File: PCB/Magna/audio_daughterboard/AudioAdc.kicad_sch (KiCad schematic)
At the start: 23 parts, among them J201 PSG01550, U201 WM8782SEDS

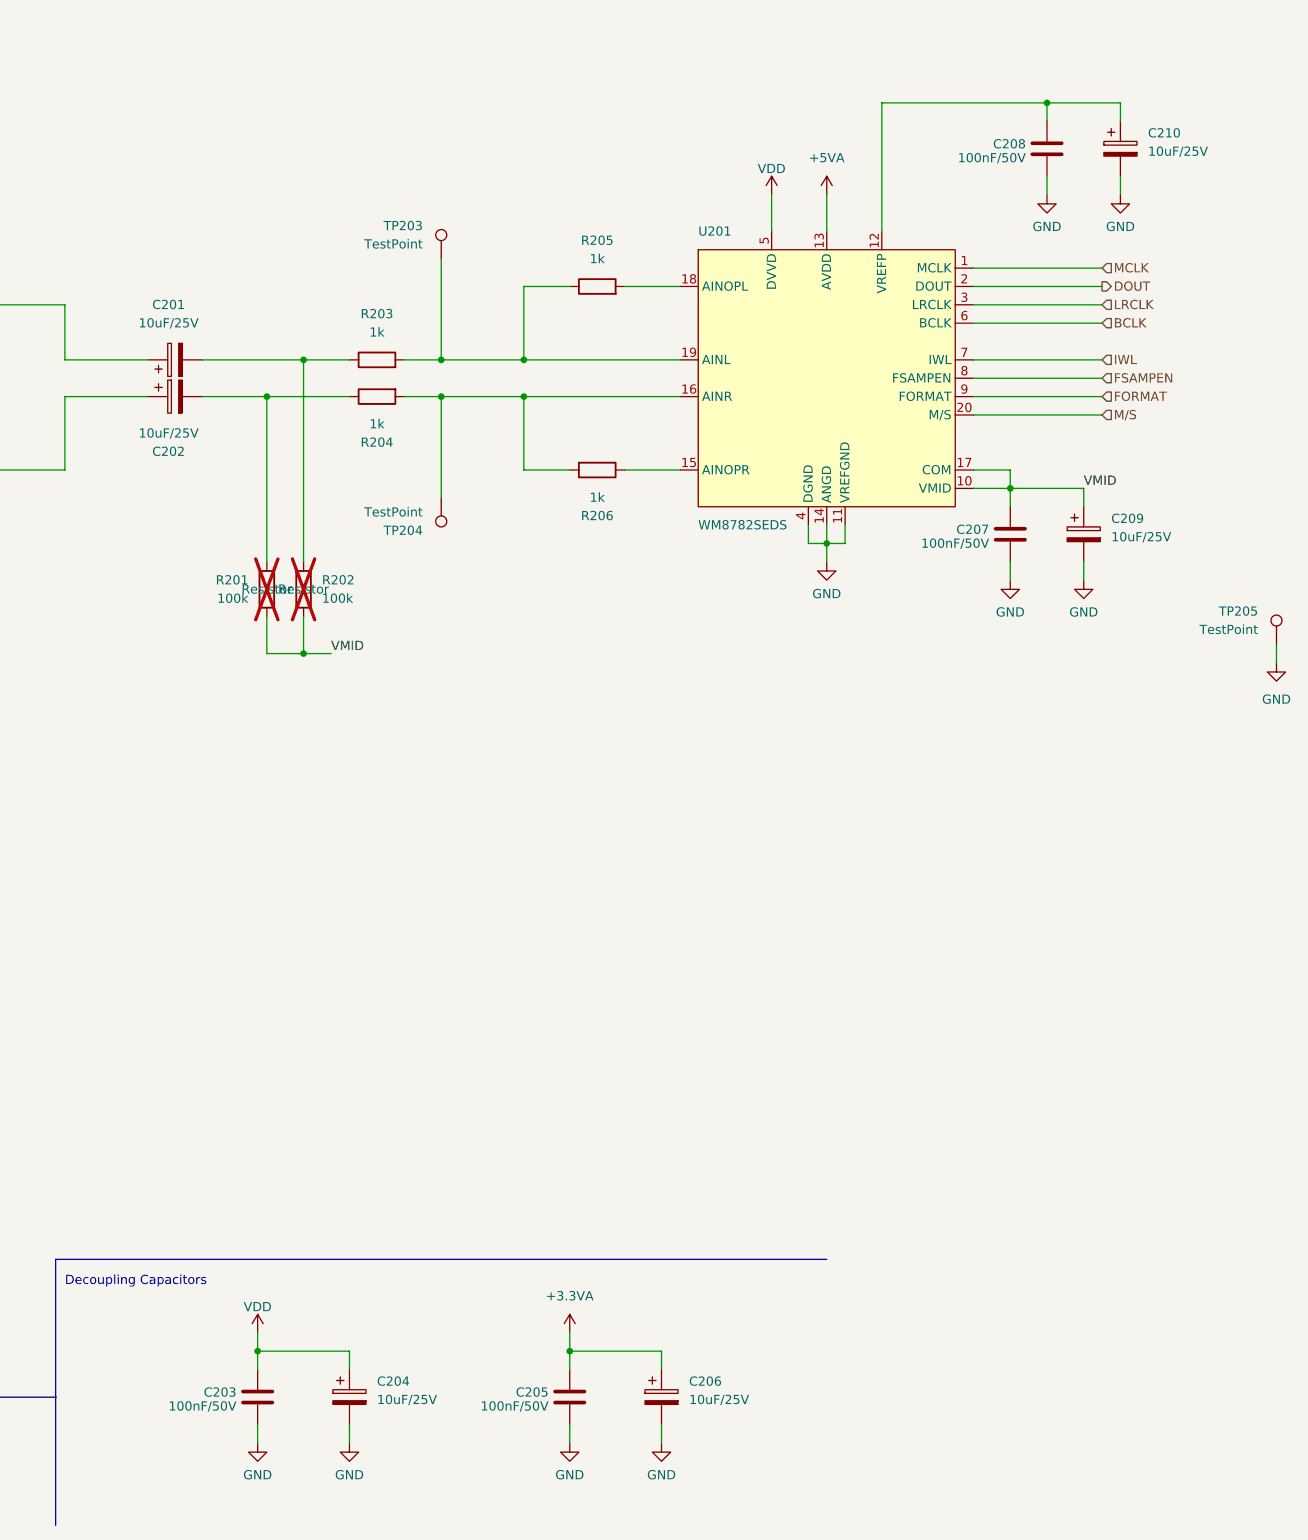
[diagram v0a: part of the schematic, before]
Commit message: Update audio PCB
Mainly added simulations to Linedriver and DAC.

Also fixed some small issues that was found when simulating
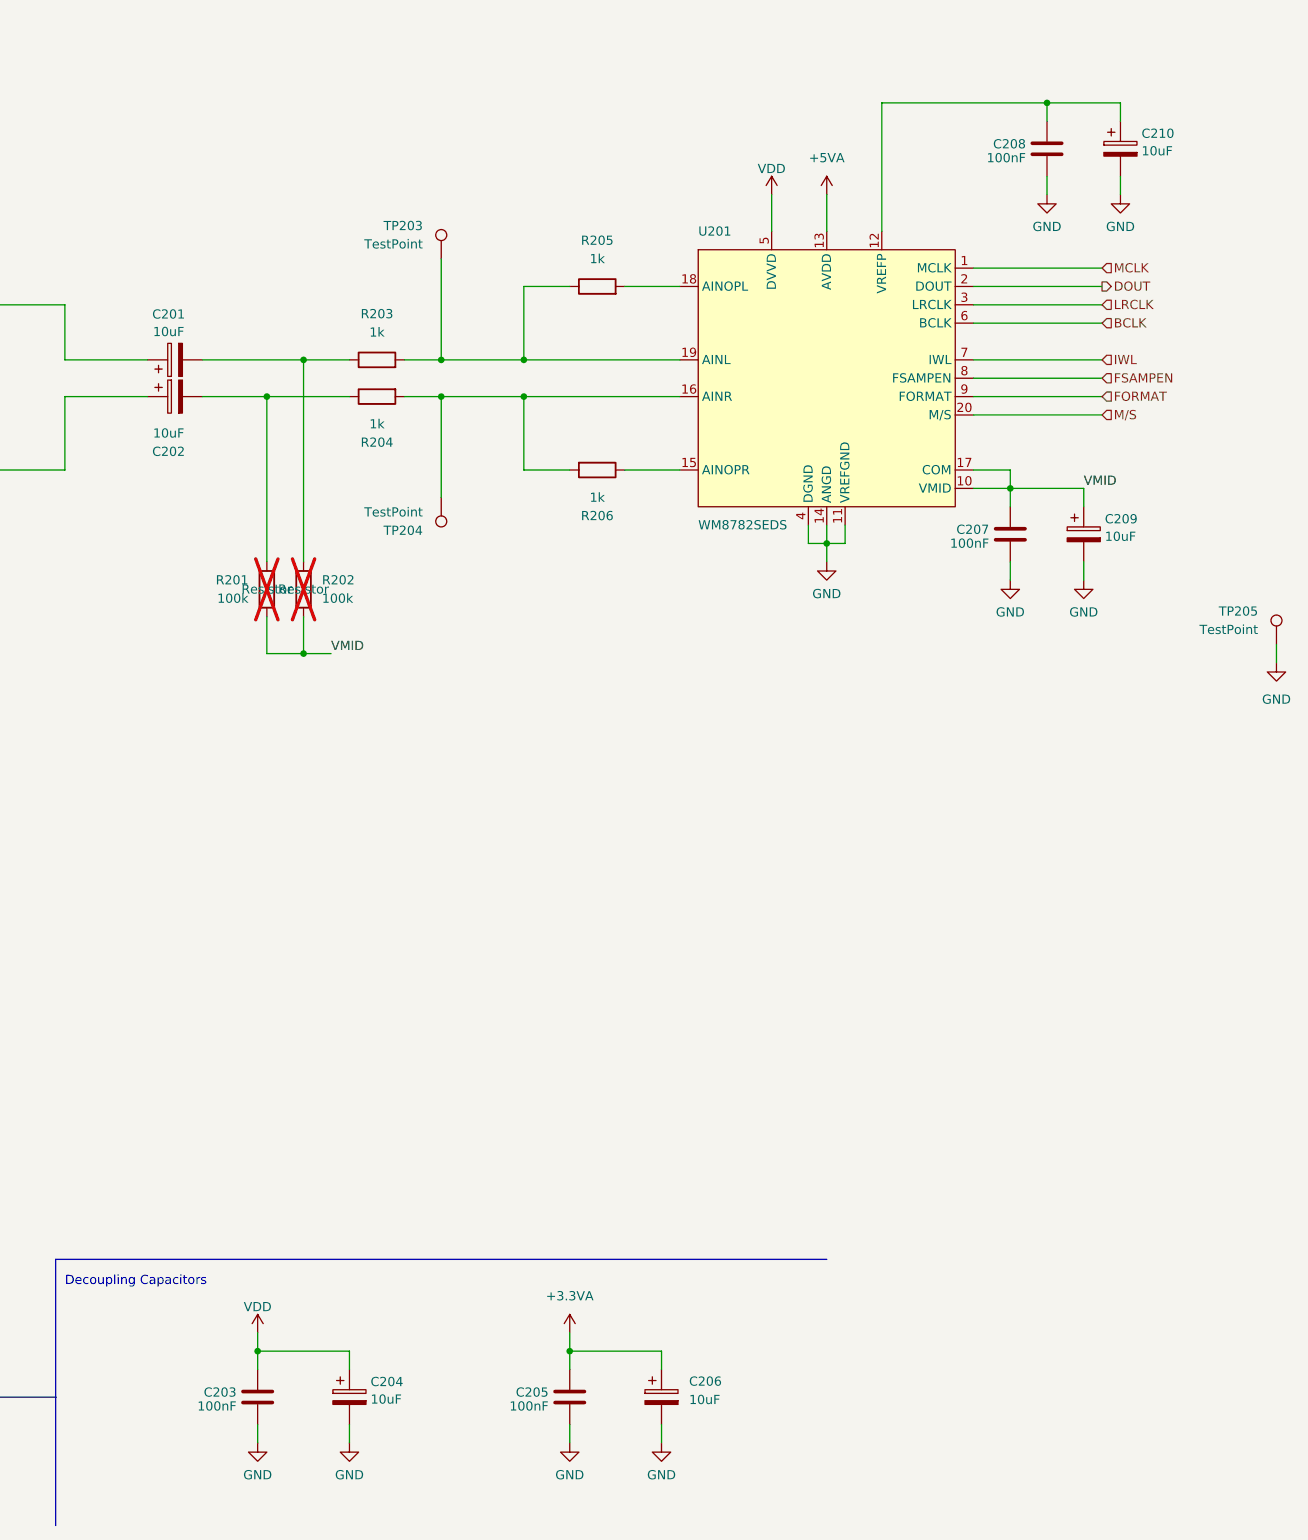
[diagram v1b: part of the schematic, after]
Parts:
- C201, C202, C204, C206, C209, C210: value 10uF/25V -> 10uF
- C203, C205, C207, C208: value 100nF/50V -> 100nF
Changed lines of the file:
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@@
 		(fields_autoplaced yes)
 		(property "Reference" "C210"
-			(at 359.41 66.421 0)
-			(effects
-				(font
-					(size 1.27 1.27)
-				)
-				(justify left)
-			)
-		)
-		(property "Value" "10uF/25V"
-			(at 359.41 68.961 0)
+			(at 358.521 66.4788 0)
+			(effects
+				(font
+					(size 1.27 1.27)
+				)
+				(justify left)
+			)
+		)
+		(property "Value" "10uF"
+			(at 358.521 68.9031 0)
 			(effects
 				(font
@@
 			)
 		)
-		(property "Value" "100nF/50V"
+		(property "Value" "100nF"
 			(at 342.519 69.8573 0)
 			(effects
@@
 			)
 		)
-		(property "Value" "100nF/50V"
+		(property "Value" "100nF"
 			(at 276.479 242.5773 0)
 			(effects
@@
 			)
 		)
-		(property "Value" "10uF/25V"
+		(property "Value" "10uF"
 			(at 295.91 241.681 0)
 			(effects
@@
 		(fields_autoplaced yes)
 		(property "Reference" "C201"
-			(at 223.901 90.17 90)
-			(effects
-				(font
-					(size 1.27 1.27)
-				)
-			)
-		)
-		(property "Value" "10uF/25V"
-			(at 223.901 92.71 90)
+			(at 223.901 91.4865 90)
+			(effects
+				(font
+					(size 1.27 1.27)
+				)
+			)
+		)
+		(property "Value" "10uF"
+			(at 223.901 93.9108 90)
 			(effects
 				(font
@@
 			)
 		)
-		(property "Value" "100nF/50V"
+		(property "Value" "100nF"
 			(at 337.439 123.1973 0)
 			(effects
@@
 			)
 		)
-		(property "Value" "10uF/25V"
+		(property "Value" "10uF"
 			(at 223.901 107.95 90)
 			(effects
@@
 		(fields_autoplaced yes)
 		(property "Reference" "C204"
-			(at 252.73 239.141 0)
-			(effects
-				(font
-					(size 1.27 1.27)
-				)
-				(justify left)
-			)
-		)
-		(property "Value" "10uF/25V"
-			(at 252.73 241.681 0)
+			(at 251.841 239.1988 0)
+			(effects
+				(font
+					(size 1.27 1.27)
+				)
+				(justify left)
+			)
+		)
+		(property "Value" "10uF"
+			(at 251.841 241.6231 0)
 			(effects
 				(font
@@
 			)
 		)
-		(property "Value" "100nF/50V"
+		(property "Value" "100nF"
 			(at 233.299 242.5773 0)
 			(effects
@@
 		(fields_autoplaced yes)
 		(property "Reference" "C209"
-			(at 354.33 119.761 0)
-			(effects
-				(font
-					(size 1.27 1.27)
-				)
-				(justify left)
-			)
-		)
-		(property "Value" "10uF/25V"
-			(at 354.33 122.301 0)
-			(effects
-				(font
+			(at 353.441 119.8188 0)
+			(effects
+				(font
+					(size 1.27 1.27)
+				)
+				(justify left)
+			)
+		)
+		(property "Value" "10uF"
+			(at 353.441 122.2431 0)
+			(effects
+				(font

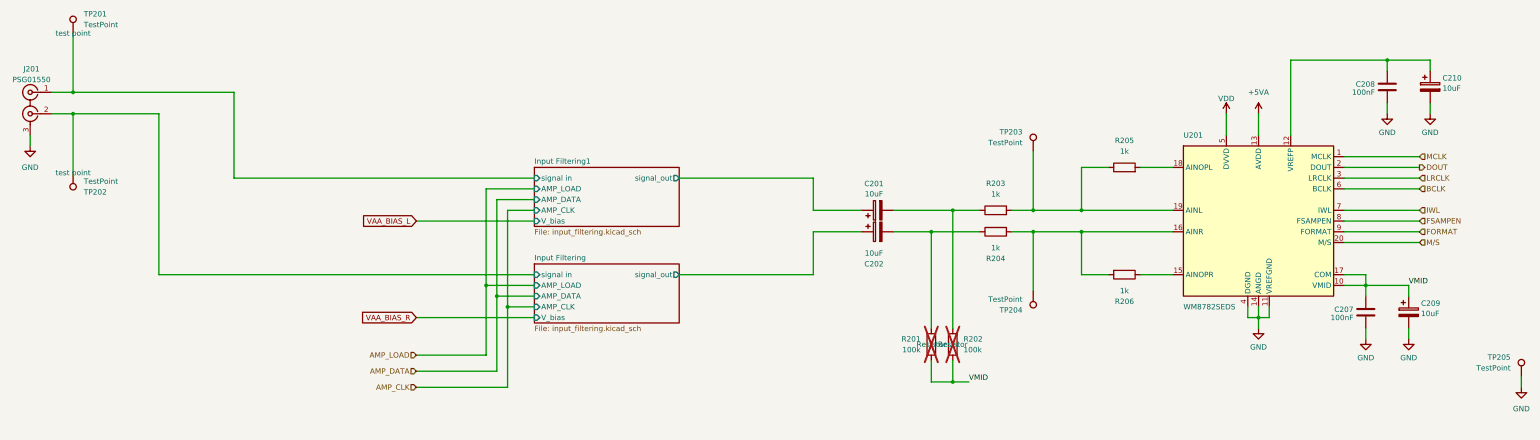
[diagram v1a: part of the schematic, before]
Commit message: "Finalize" Audio daugherboard
Finished DAC output filter
Fixed the whole damn MCU subschematic
Fixed Linedriver schematic
Added component footprints and LCSC numbers
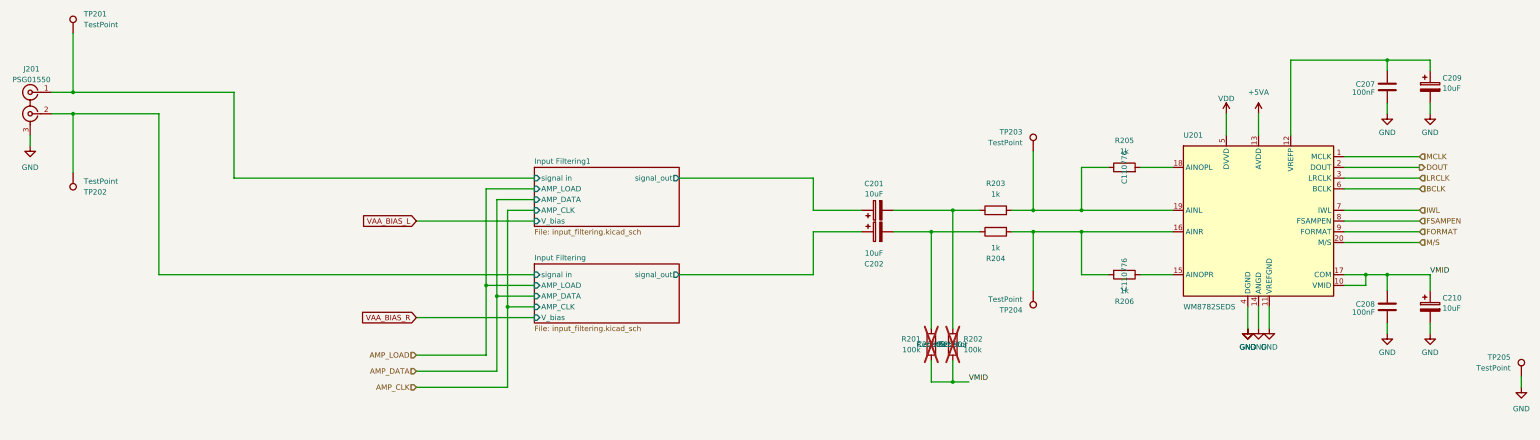
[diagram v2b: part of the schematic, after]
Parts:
- C201, C202, C203, C204, C205, C206, J201, TP201, TP202, TP203, TP204, TP205, U201: now left out of the parts list
- C207: renamed from C208; now left out of the parts list
- C208: renamed from C207; now left out of the parts list
- C209: renamed from C210; now left out of the parts list
- C210: renamed from C209; now left out of the parts list
- R201, R202: footprint (none) -> Resistor_SMD:R_0603_1608Metric; LCSC (none) -> C25803
- R203, R204, R205, R206: footprint (none) -> Resistor_SMD:R_0603_1608Metric; LCSC (none) -> C110776; now left out of the parts list
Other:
- moved on the sheet: C208, C210

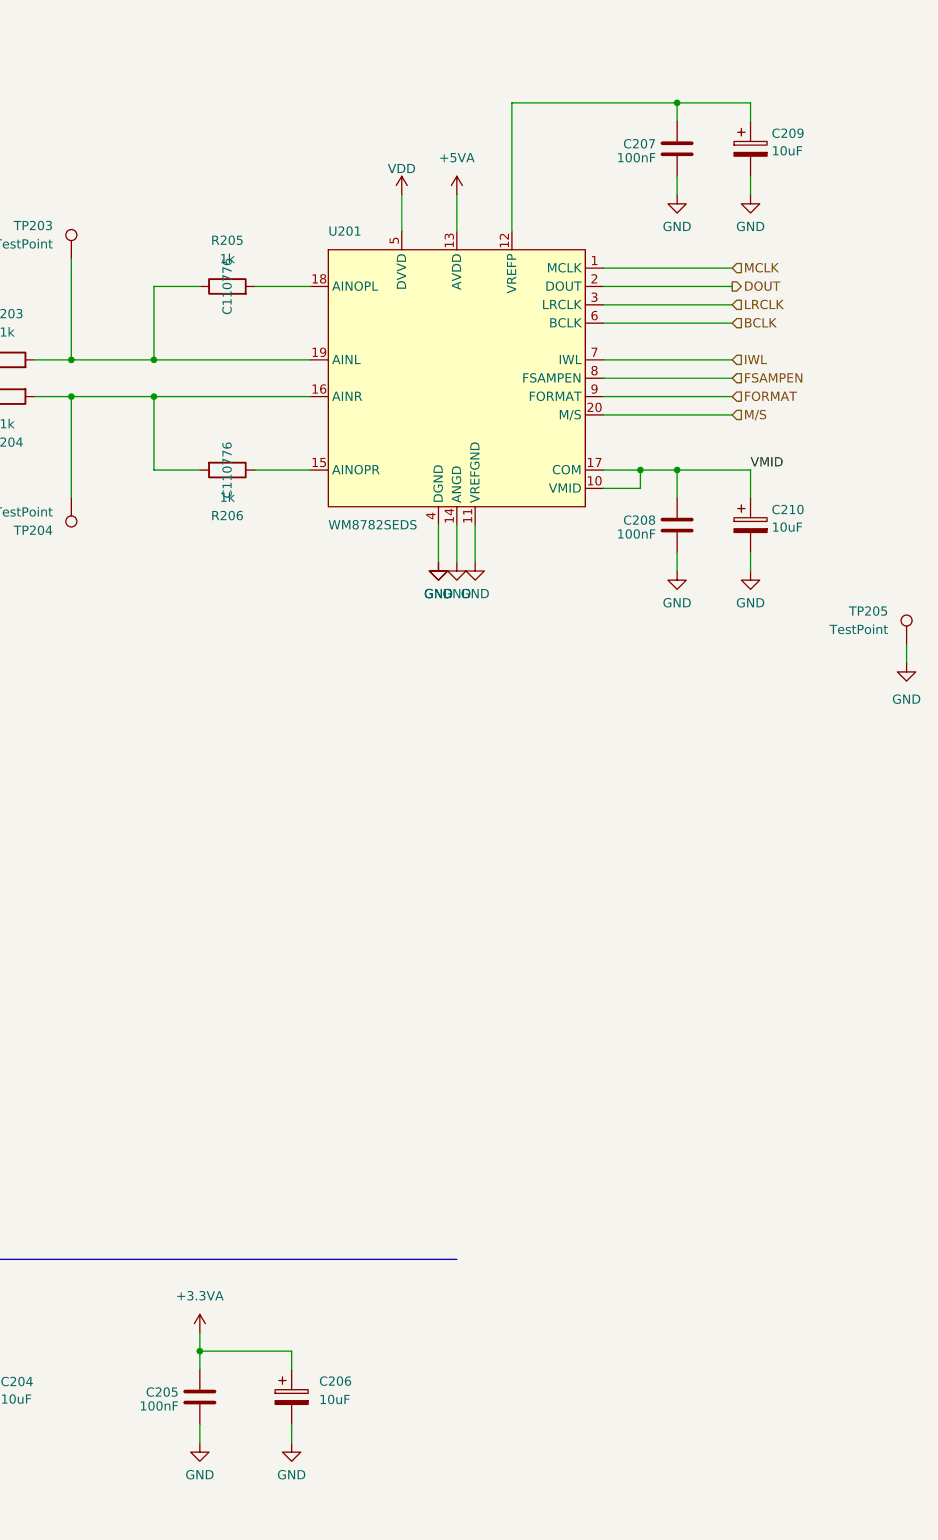
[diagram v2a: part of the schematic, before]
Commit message: Do most of the component placement for audio board
Just a general layout, things will probably change
as the routing begins.
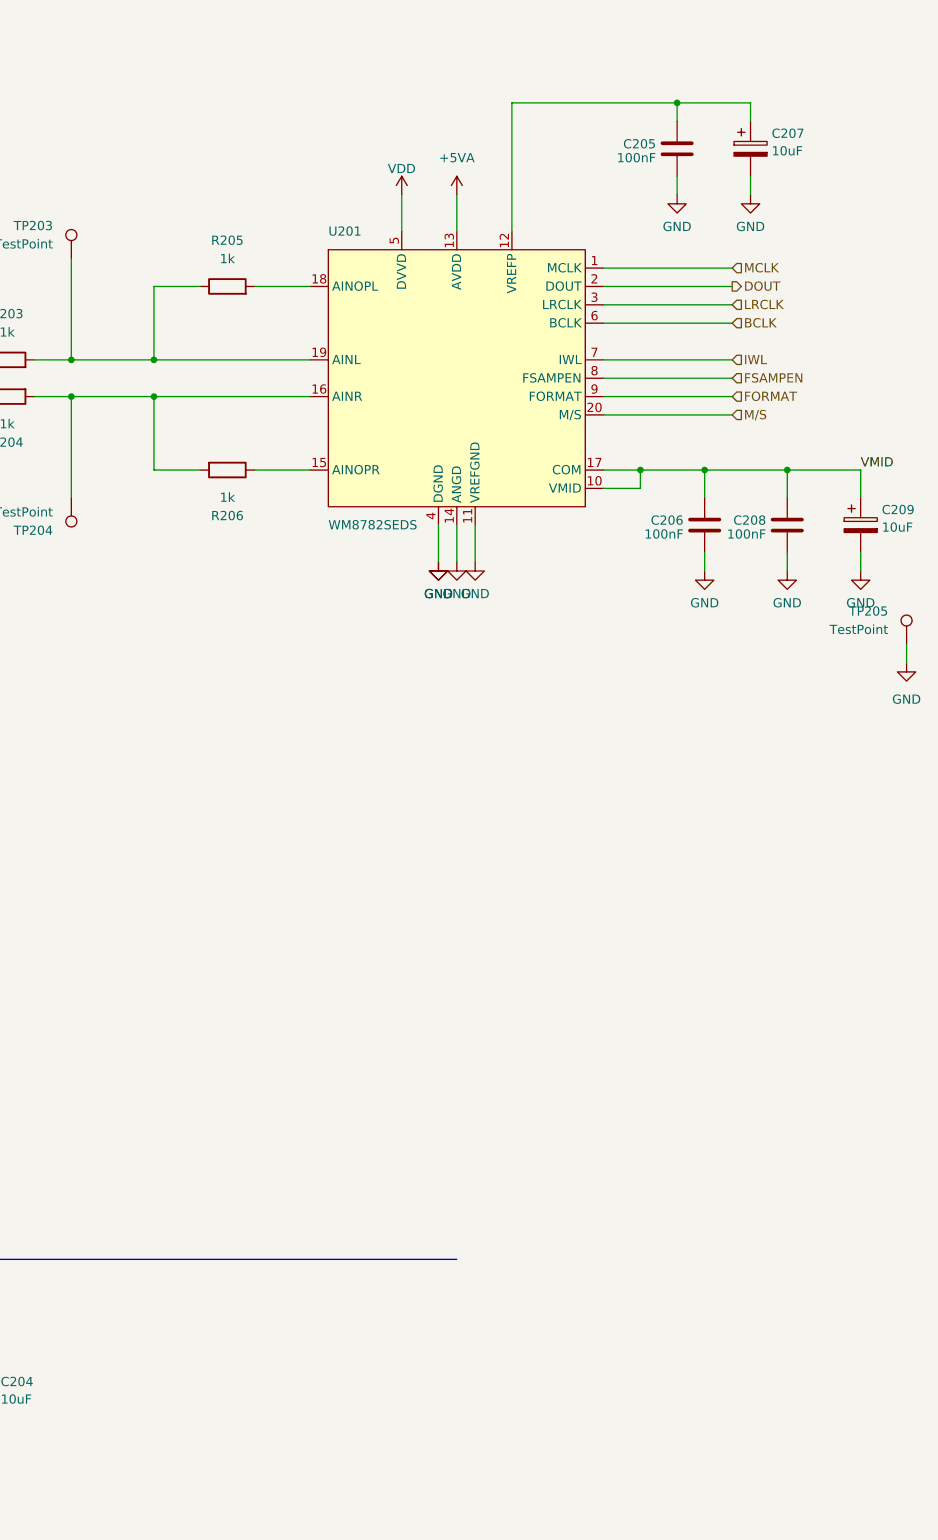
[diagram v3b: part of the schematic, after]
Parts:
- removed C205: 100nF, Capacitor_SMD:C_0805_2012Metric_Pad1.18x1.45mm_HandSolder, symbol Device:C
- removed C206: 10uF, Capacitor_SMD:CP_Elec_4x5.8, symbol Device:C_Polarized
- added C206: 100nF, Capacitor_SMD:C_0603_1608Metric, symbol Device:C
- C203, C208: footprint Capacitor_SMD:C_0805_2012Metric_Pad1.18x1.45mm_HandSolder -> Capacitor_SMD:C_0603_1608Metric; LCSC C49678 -> C14663
- C205: renamed from C207; footprint Capacitor_SMD:C_0805_2012Metric_Pad1.18x1.45mm_HandSolder -> Capacitor_SMD:C_0603_1608Metric; LCSC C49678 -> C14663
- renumbered C209 to C207, C210 to C209
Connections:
- net GND: now also C206.2
- net VMID: now also C206.1
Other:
- moved on the sheet: C208, C209
